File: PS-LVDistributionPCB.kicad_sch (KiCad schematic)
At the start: 1 part, among them J15 Conn_01x20

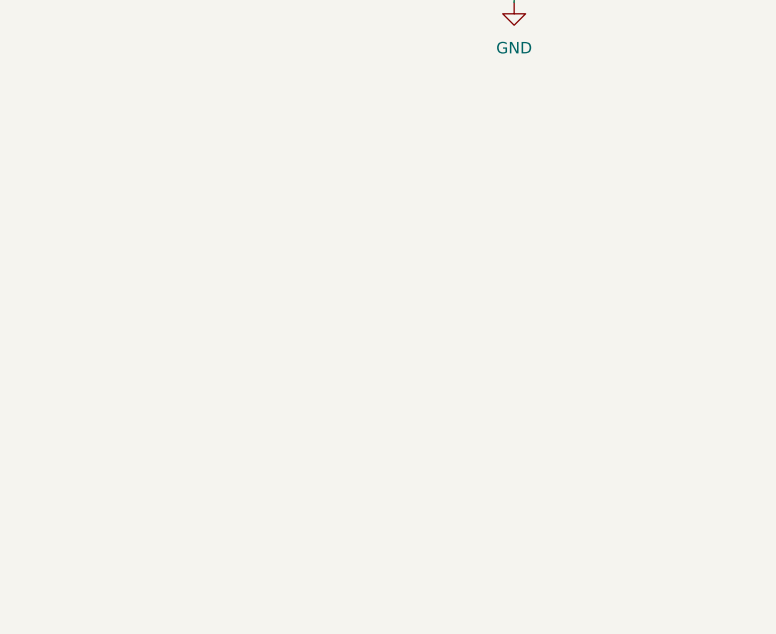
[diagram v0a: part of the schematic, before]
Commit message: added TVS diodes and routed traces
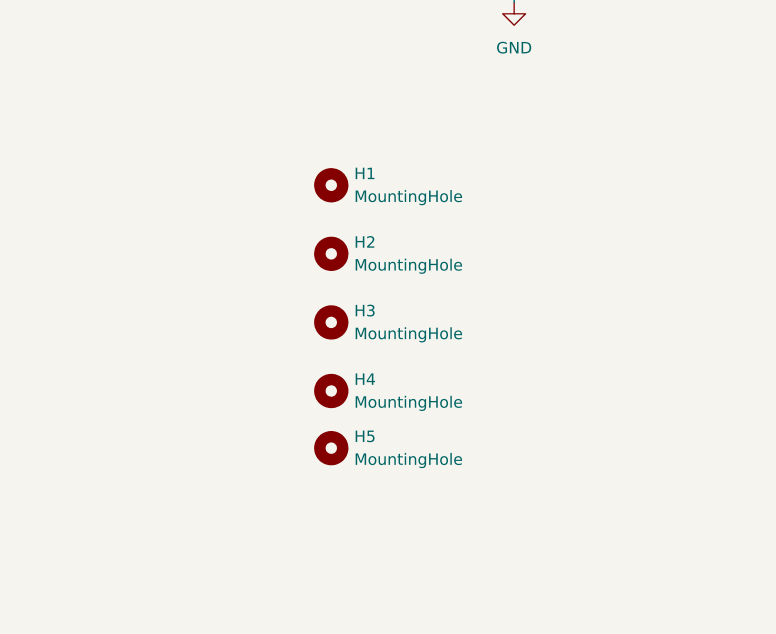
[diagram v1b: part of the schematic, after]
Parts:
- added H1, H2, H3, H4, H5: MountingHole, MountingHole:MountingHole_3.2mm_M3, symbol Mechanical:MountingHole

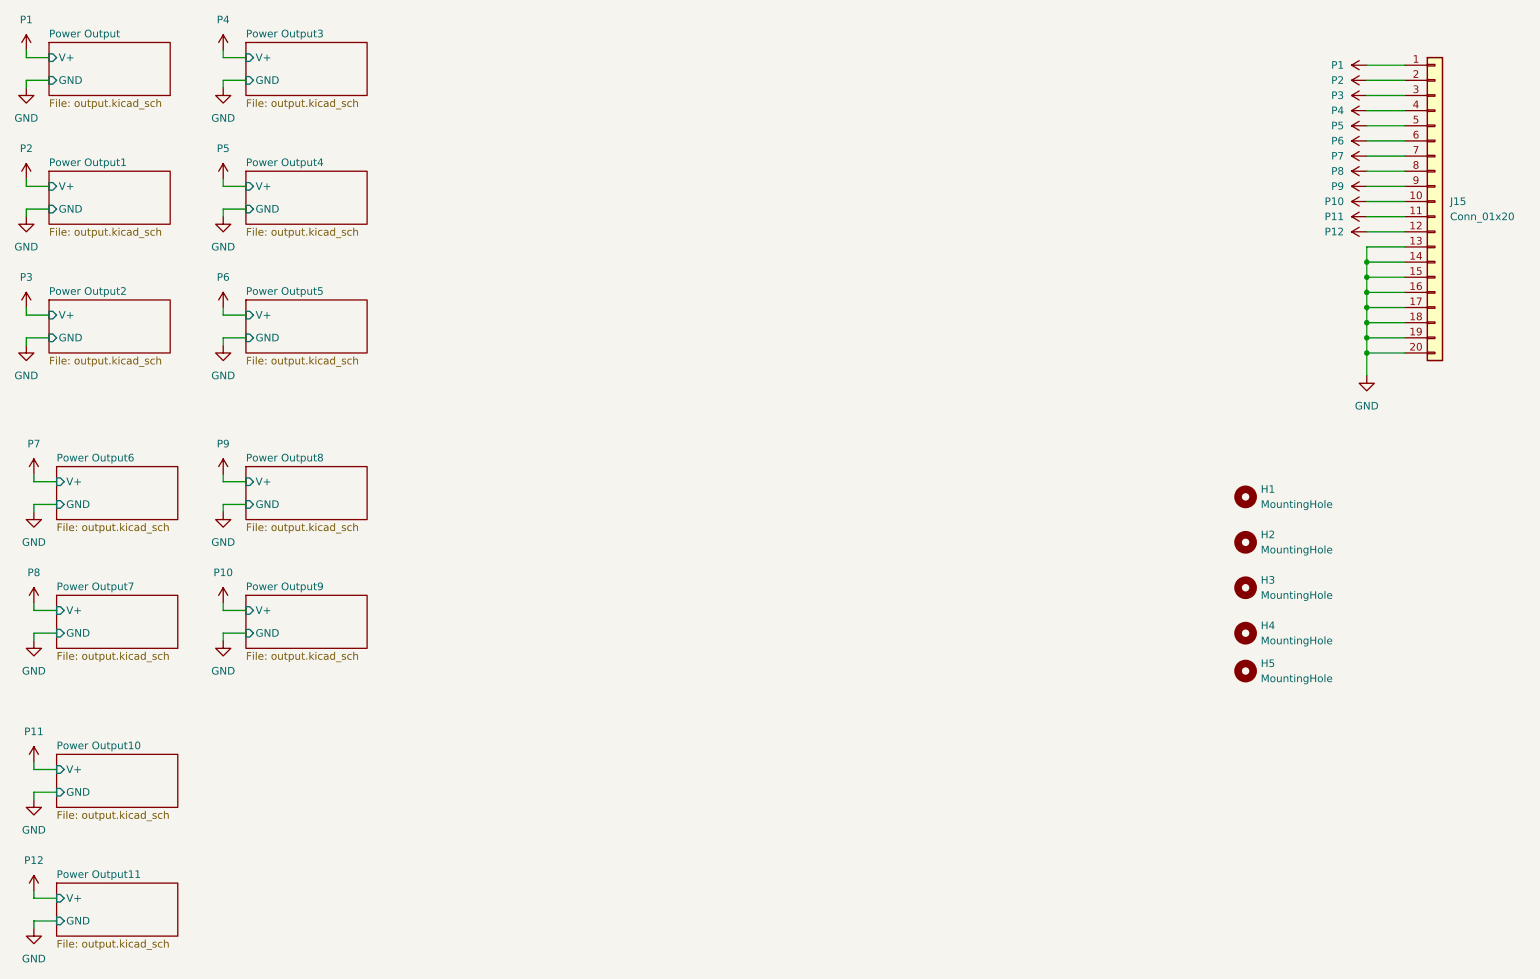
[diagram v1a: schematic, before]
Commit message: 14 outputs with 2 row mx150 symbol
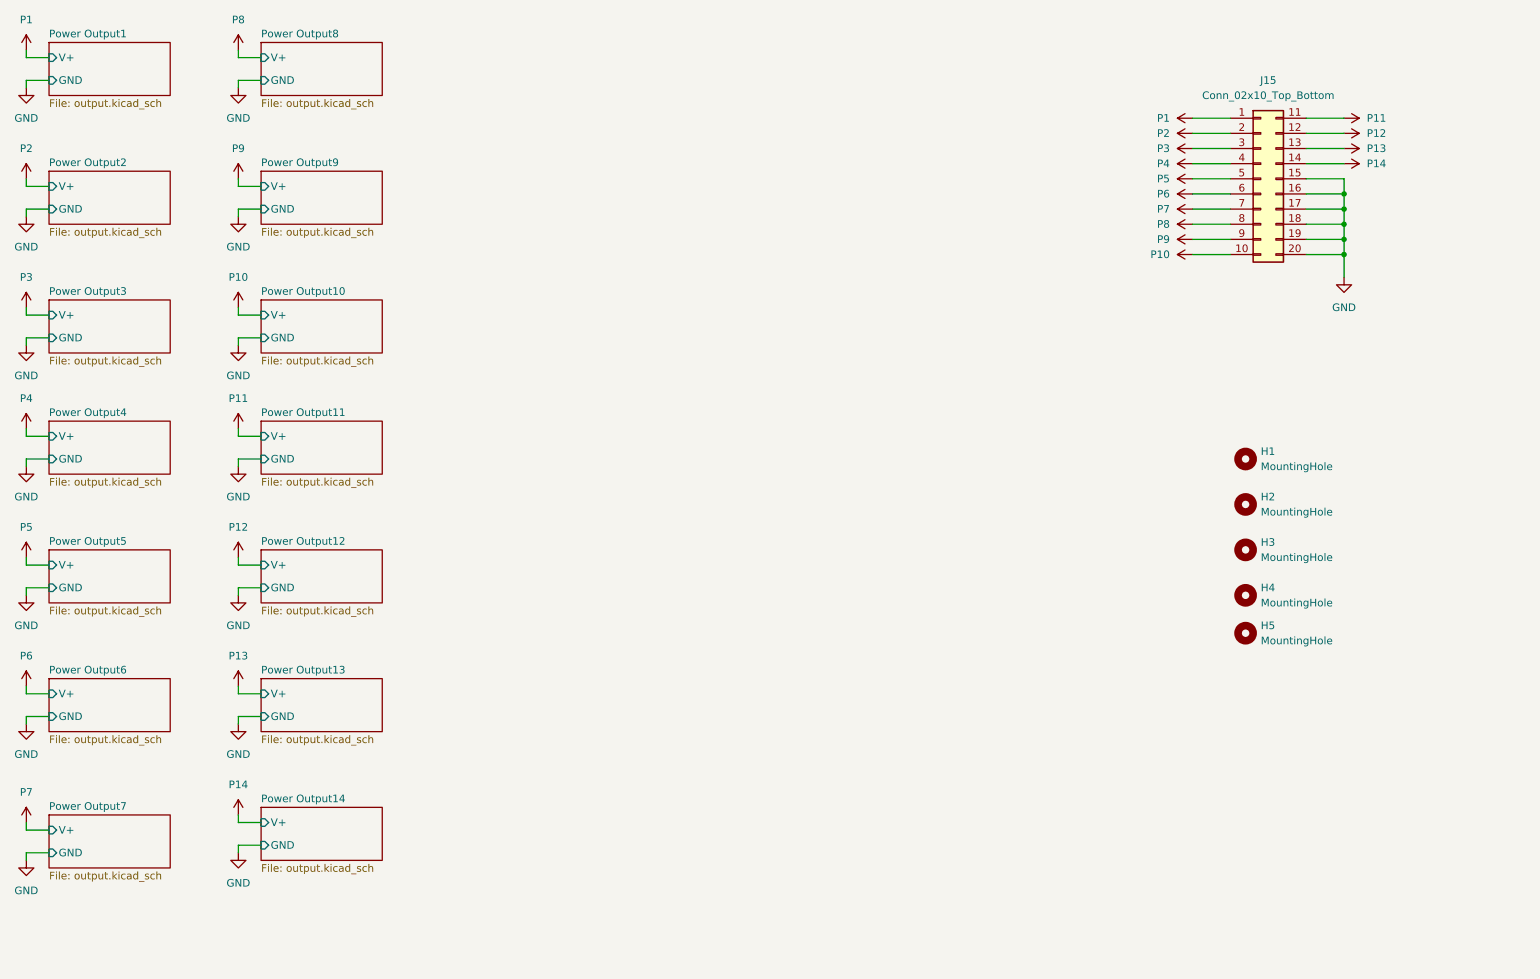
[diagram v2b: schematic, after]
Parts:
- removed J15: Conn_01x20, footprints:CONN_SD-34829-001_20_ST_MOL, symbol Connector_Generic:Conn_01x20
- added J15: Conn_02x10_Top_Bottom, footprints:CONN_SD-34829-001_20_ST_MOL, symbol Connector_Generic:Conn_02x10_Top_Bottom
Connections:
- net GND: now also J15.15 (Pin_15), J15.16 (Pin_16), J15.17 (Pin_17), J15.18 (Pin_18), J15.19 (Pin_19), J15.20 (Pin_20)
- net P1: now also J15.1 (Pin_1)
- net P10: now also J15.10 (Pin_10)
- net P11: now also J15.11 (Pin_11)
- net P12: now also J15.12 (Pin_12)
- net P2: now also J15.2 (Pin_2)
- net P3: now also J15.3 (Pin_3)
- net P4: now also J15.4 (Pin_4)
- net P5: now also J15.5 (Pin_5)
- net P6: now also J15.6 (Pin_6)
- net P7: now also J15.7 (Pin_7)
- net P8: now also J15.8 (Pin_8)
- net P9: now also J15.9 (Pin_9)
- new net P13: J15.13 (Pin_13)
- new net P14: J15.14 (Pin_14)
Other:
- removed sheet Power Output
- added sheet Power Output12 (output.kicad_sch)
- added sheet Power Output13 (output.kicad_sch)
- added sheet Power Output14 (output.kicad_sch)
- moved on the sheet: H1, H2, H3, H4, H5
